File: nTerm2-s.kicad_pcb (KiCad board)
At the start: 2 copper layers, 147.3 x 55.9 mm, 107 parts, among them J1 VGA, J2 Keyboard, J3 Mouse, J4 Speaker, J5 DE9_Plug_MountingHoles, J6 USB_C_Receptacle_USB2.0_16P, K1 IM41 3V, K2 IM41 3V, K3 IM41 3V, Q1 BC817, Q2 BC817, Q3 BC817, Q4 BC817, Q5 BC817, SW1 IO0, SW2 RESET, SW3 DEFAULTS, U1 ESP32-WROOM-32, U2 LM386, U3 MAX3232E, U4 CP2102N-Axx-xQFN28, U5 NCP1117-3.3_SOT223

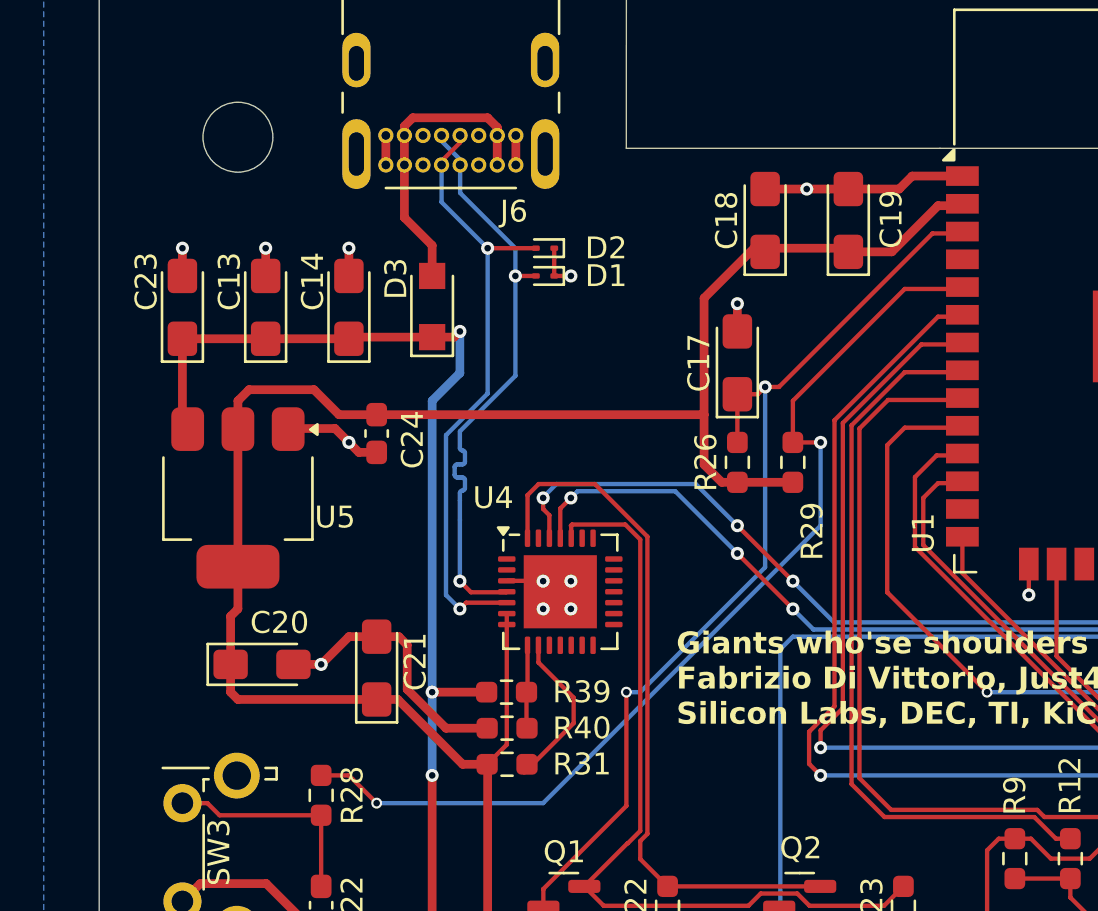
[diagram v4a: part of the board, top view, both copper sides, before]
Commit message: Fix all tantalum capacitor sizes.
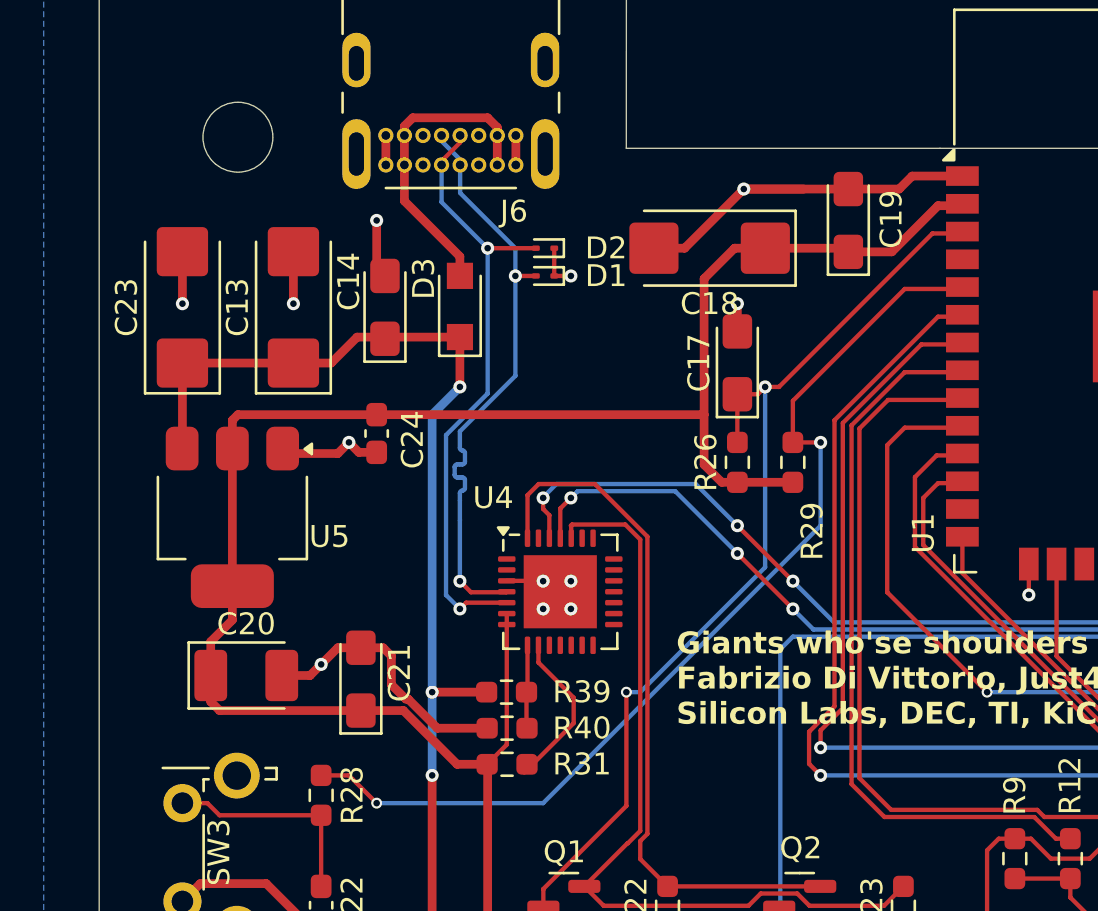
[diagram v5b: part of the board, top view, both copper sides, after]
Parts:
- C13, C18, C23: footprint Capacitor_Tantalum_SMD:CP_EIA-3216-18_Kemet-A_Pad1.58x1.35mm_HandSolder -> Capacitor_Tantalum_SMD:CP_EIA-6032-28_Kemet-C_Pad2.25x2.35mm_HandSolder
- C20: value 10u/25v -> 10u; footprint Capacitor_Tantalum_SMD:CP_EIA-3216-18_Kemet-A_Pad1.58x1.35mm_HandSolder -> Capacitor_Tantalum_SMD:CP_EIA-3528-21_Kemet-B_Pad1.50x2.35mm_HandSolder
- C21: value 0.1u/25v -> 0.1u
- moved C18 2.84 mm to (55.9, 41.9), turned to 180 degrees
- moved C14 1.65 mm to (41.0, 44.6)
- moved D3 1.27 mm to (44.5, 44.6)
- moved C13 1.27 mm to (36.8, 44.6)
- moved U5 0.92 mm to (34.0, 54.2)
- moved C20 0.88 mm to (34.7, 61.5)
- moved C21 0.88 mm to (39.9, 61.6)
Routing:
- net GND: track 169.9 -> 182.0 mm
- net +3V3: track 254.1 -> 254.9 mm
- net Net-(D3-A): track 13.7 -> 14.2 mm

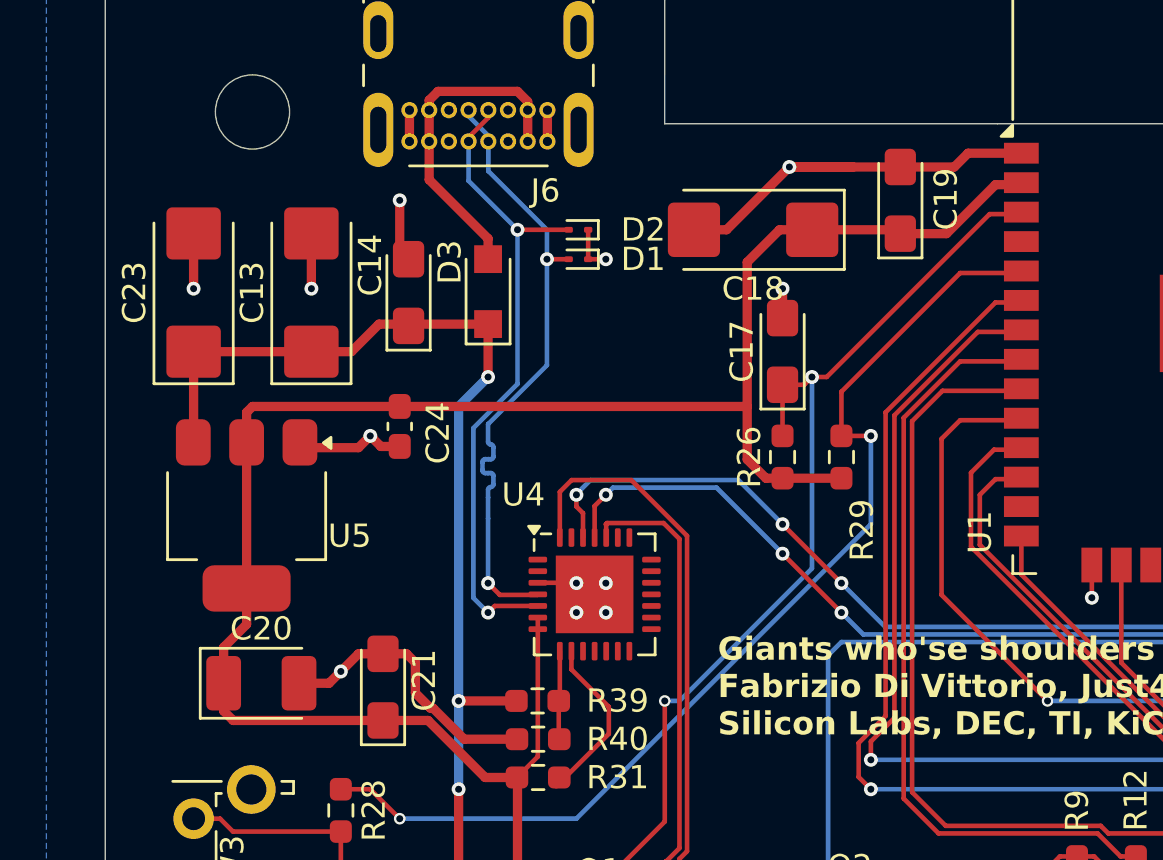
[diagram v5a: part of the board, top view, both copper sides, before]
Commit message: Some small replacements, doublechecked size of tiny ESD protectors, but they are really *tiny*. Set them further apart, so maybe they are easier to solder this way.
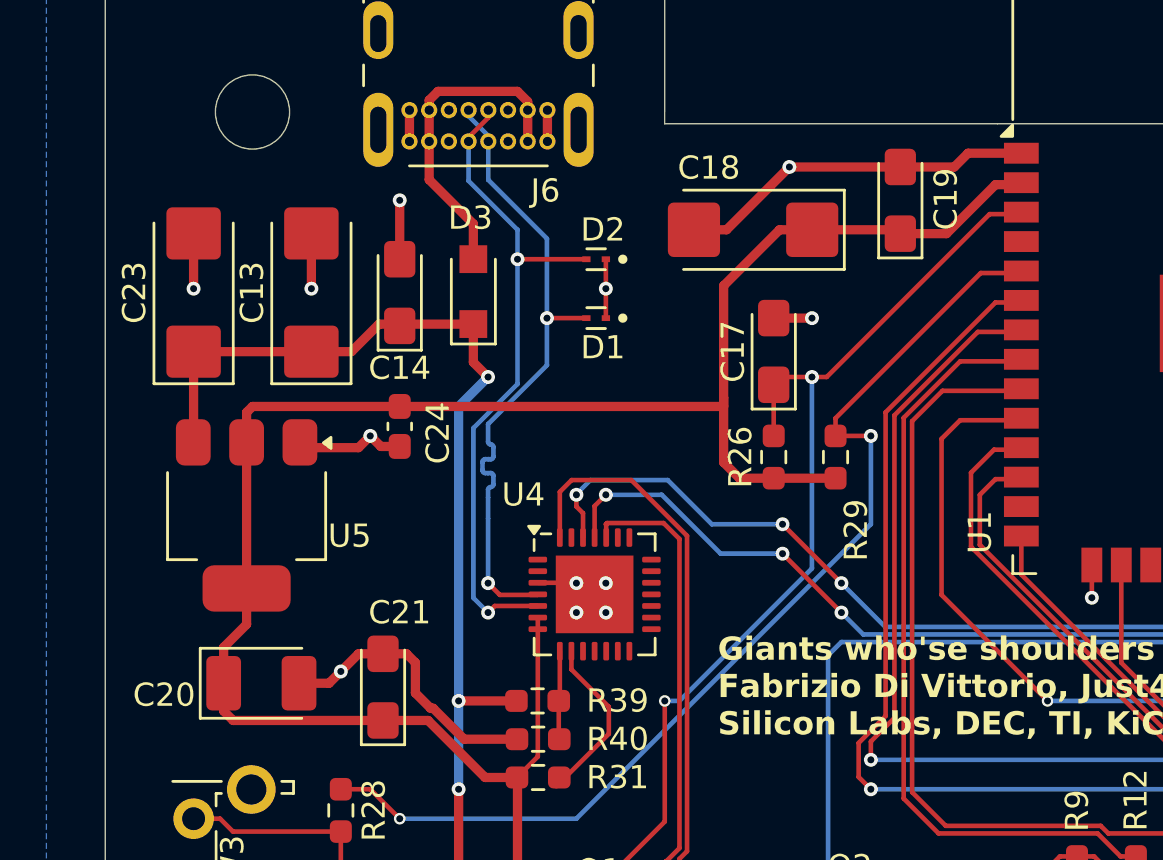
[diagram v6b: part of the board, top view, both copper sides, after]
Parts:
- D1, D2: footprint Diode_SMD:D_SOD-923 -> ESD9D5.0ST5G:TVS_ESD9D5.0ST5G
- moved D1 2.65 mm to (49.1, 45.7)
- moved D2 1.48 mm to (49.1, 43.2)
- moved D3 0.64 mm to (43.8, 44.6)
- moved C14 0.38 mm to (40.6, 44.6)
- moved C17 0.38 mm to (56.8, 47.2)
- moved R26 0.38 mm to (56.8, 51.7)
- moved R29 0.25 mm to (59.4, 51.7)
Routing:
- net GND: track 182.0 -> 180.1 mm
- net Net-(D2-A2): track 28.4 -> 29.2 mm
- net Net-(D1-A2): track 27.1 -> 27.9 mm
- net +3V3: track 254.9 -> 255.5 mm

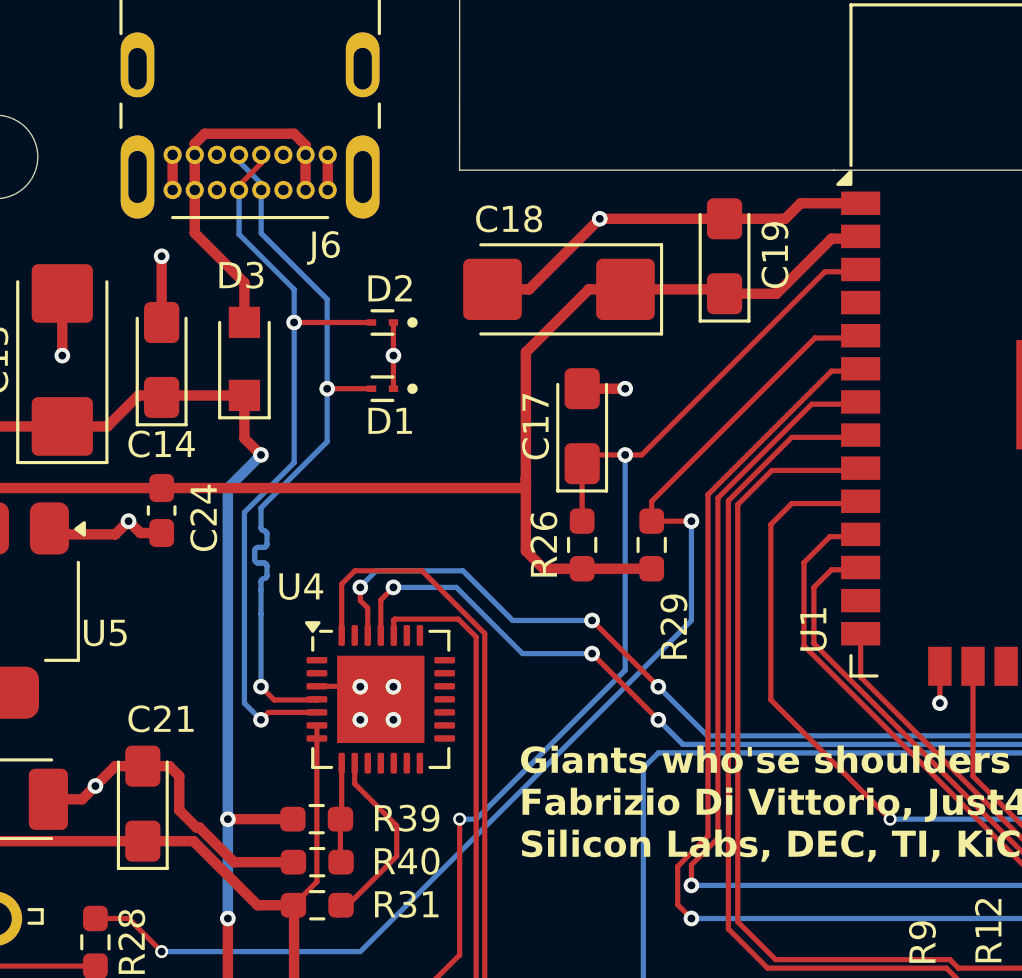
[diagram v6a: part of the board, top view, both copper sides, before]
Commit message: Use other TVS protection diodes, with a hand-solderable size.
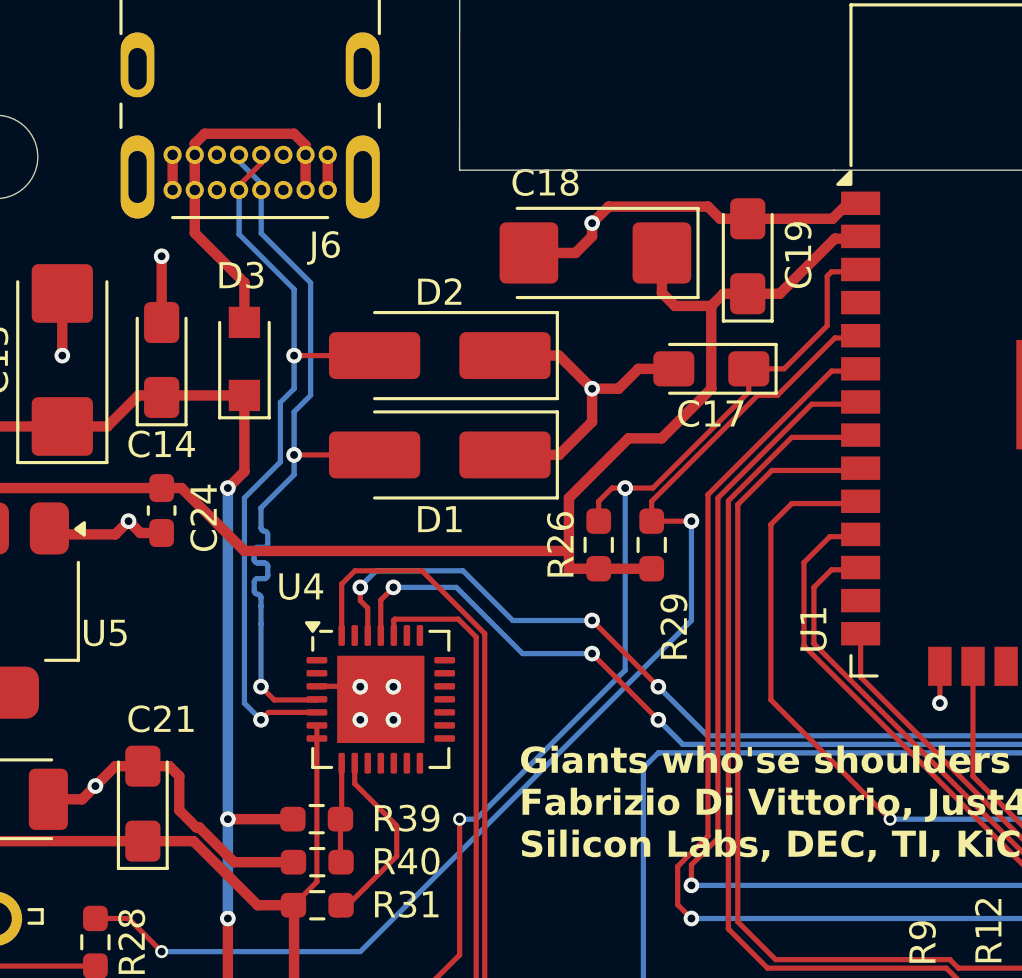
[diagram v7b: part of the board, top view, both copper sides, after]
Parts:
- D1, D2: value ESD9B5.0ST5G -> P4SMAJ5.0CA; footprint ESD9D5.0ST5G:TVS_ESD9D5.0ST5G -> Diode_SMD:D_SMA_Handsoldering
- moved C17 5.42 mm to (61.7, 45.0), turned to 180 degrees
- moved D1 3.36 mm to (51.3, 48.3)
- moved D2 2.54 mm to (51.3, 44.5)
- moved C18 1.98 mm to (57.3, 40.5)
- moved C19 0.89 mm to (63.1, 40.6)
- moved R26 0.64 mm to (57.4, 51.7)
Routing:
- net GND: track 180.1 -> 187.1 mm, vias 19 -> 18
- net +3V3: track 255.5 -> 257.1 mm
- net Net-(D1-A2): track 27.9 -> 29.3 mm
- net EN: track 48.5 -> 47.4 mm
- net +5V: track 250.4 -> 249.8 mm

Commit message: More small improvements to layout.
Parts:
- C25, C26, C27: footprint Capacitor_Tantalum_SMD:CP_EIA-3216-18_Kemet-A_Pad1.58x1.35mm_HandSolder -> Capacitor_SMD:CP_Elec_6.3x7.7
- D1, D2: footprint Diode_SMD:D_SMA_Handsoldering -> Diode_SMD:D_SMA
- K1, K2, K3: footprint Relay_SMD:Relay_2P2T_10x6mm_TE_IMxxG -> Relay_SMD:Relay_DPDT_AXICOM_IMSeries_Gullwing
- moved C12 62.4 mm to (161.4, 101.9)
- moved C25 62.2 mm to (206.7, 120.4)
- moved C10 62.1 mm to (147.6, 106.8)
- moved C9 62.1 mm to (144.5, 106.8)
- moved D1 62.1 mm to (97.5, 89.7)
- moved R1 62.1 mm to (139.9, 86.4)
- moved R15 62.1 mm to (128.7, 111.3)
- moved R4 62.1 mm to (139.9, 88.2)
- moved R6 62.1 mm to (139.9, 91.8)
- moved R8 62.1 mm to (139.9, 80.9)
- moved R9 62.1 mm to (116.0, 111.3)
- moved SW1 62.1 mm to (110.9, 124.0)
- moved C11 62.1 mm to (147.6, 101.2), turned to -90 degrees
- moved C15 62.1 mm to (110.6, 117.7)
- moved C16 62.1 mm to (99.3, 117.7)
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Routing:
- net +5V: track 249.8 -> 190.0 mm
- net RTS_OR_DTR_RLY_-: track 28.0 -> 12.2 mm
- net /_RTS: track 18.5 -> 29.3 mm, vias 1 -> 0
- net Net-(D7-K): track 12.6 -> 21.5 mm
- net Net-(D9-K): track 12.9 -> 21.6 mm
- net Net-(D5-K): track 13.1 -> 21.6 mm
- net /CTS: track 44.5 -> 36.1 mm
- net RXD_2: track 101.2 -> 93.2 mm
- net /_CTS: track 13.4 -> 21.4 mm, vias 0 -> 1
- net /RTS: track 36.1 -> 28.3 mm
- net +3V3: track 257.1 -> 250.0 mm
- net /_DSR: track 20.9 -> 27.9 mm
- net AUDIO_PWM: track 72.7 -> 66.9 mm
- net CTS_2: track 96.7 -> 90.9 mm
- net /_DTR: track 24.8 -> 30.5 mm
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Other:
- board text added: "Giants who'se shoulders I stand upon: Fabrizio Di Vittorio, Just4Fun, OMRON, Espressif, Silicon Labs, DEC, TI, KiCad, JLCPCB, Hackaday."
- board text added: "© 2025 Sporos Tech"
- board text added: "₍^•_•^₎ﾉ"
- board text removed: "Giants who'se shoulders I stand upon: Fabrizio Di Vittorio, Just4Fun, OMRON, Espressif, Silicon Labs, DEC, TI, KiCad, PCBWay, Hackaday."
- board text removed: "nTerm2-S v0.03 © 2025 Sporos Tech ₍^•_•^₎ﾉ Powered by FabGL"
